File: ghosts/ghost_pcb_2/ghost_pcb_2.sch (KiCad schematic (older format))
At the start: 6 parts, among them SW1 SMT_SPDT

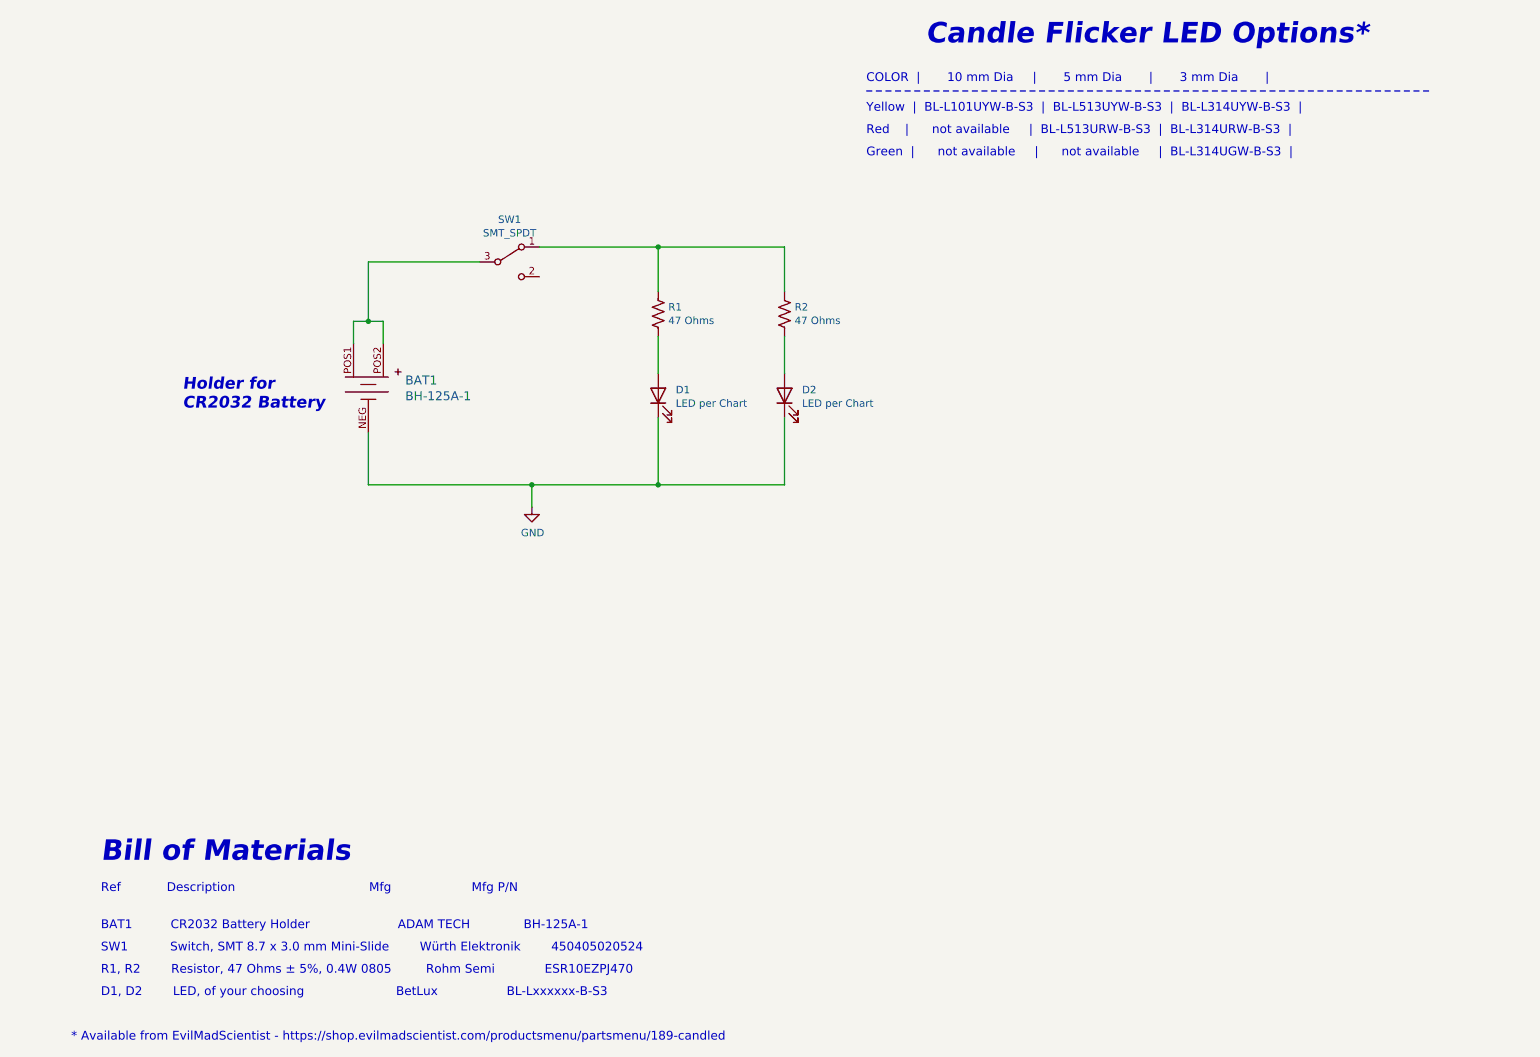
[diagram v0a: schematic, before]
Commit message: Updating all PCBS, etc.
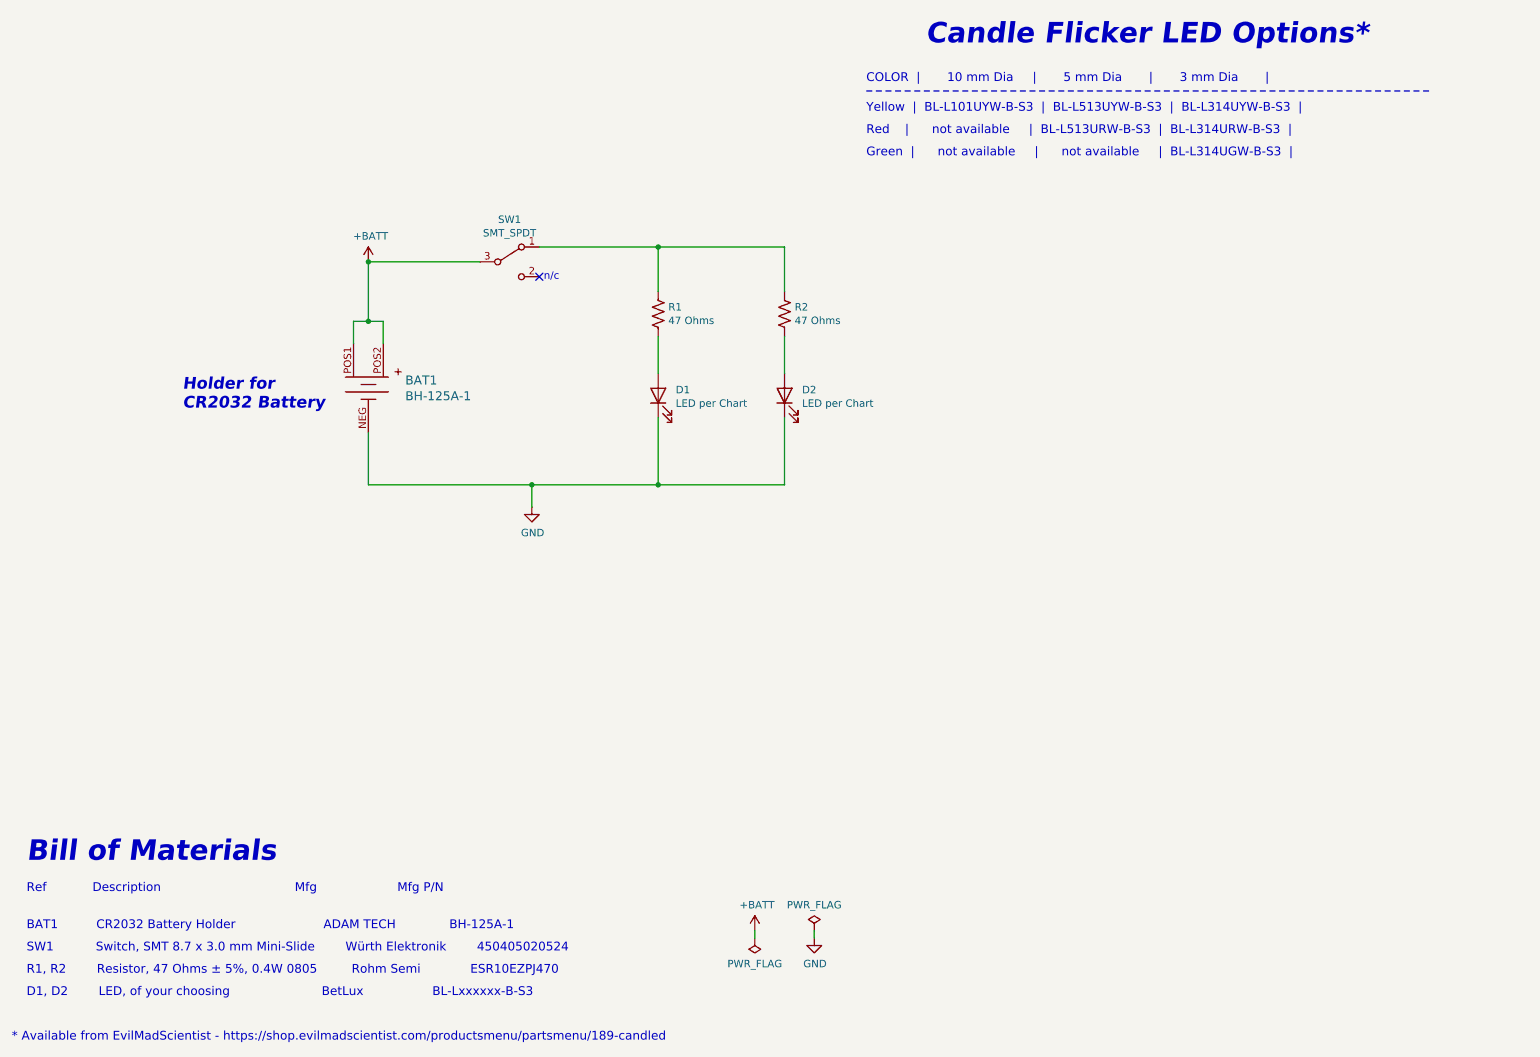
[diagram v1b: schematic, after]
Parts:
- BAT1: footprint (none) -> Battery:BatteryHolder_AdamTech_BH-125A-1
- D1, D2: footprint (none) -> LED_THT:LED_D3.0mm
- R1, R2: footprint (none) -> Resistor_SMD:R_0805_2012Metric
- SW1: footprint (none) -> Button_Switch_SMD:SMT_Mini_Slide_Switch
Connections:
- net +BATT: now reaches BAT1.POS1, BAT1.POS2, SW1.3 (B)
- no-connect marks 0 -> 1
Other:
- note added: "n/c"
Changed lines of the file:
@@
 F 0 "SW1" H 3900 2785 50  0000 C CNN
 F 1 "SMT_SPDT" H 3900 2694 50  0000 C CNN
-F 2 "" H 3900 2500 50  0001 C CNN
+F 2 "Button_Switch_SMD:SMT_Mini_Slide_Switch" H 3900 2500 50  0001 C CNN
 F 3 "" H 3900 2500 50  0001 C CNN
 	1    3900 2500
@@
 F 0 "R1" H 4968 2896 50  0000 L CNN
 F 1 "47 Ohms" H 4968 2805 50  0000 L CNN
-F 2 "" V 4940 2840 50  0001 C CNN
+F 2 "Resistor_SMD:R_0805_2012Metric" V 4940 2840 50  0001 C CNN
 F 3 "~" H 4900 2850 50  0001 C CNN
 	1    4900 2850
@@
 F 0 "D1" V 4939 3282 50  0000 R CNN
 F 1 "LED per Chart" V 4848 3282 50  0000 R CNN
-F 2 "" H 4900 3400 50  0001 C CNN
+F 2 "LED_THT:LED_D3.0mm" H 4900 3400 50  0001 C CNN
 F 3 "~" H 4900 3400 50  0001 C CNN
 	1    4900 3400
@@
 F 0 "BAT1" V 2897 3598 60  0000 L CNN
 F 1 "BH-125A-1" V 3003 3598 60  0000 L CNN
-F 2 "" H 3150 3550 60  0001 L CNN
+F 2 "Battery:BatteryHolder_AdamTech_BH-125A-1" H 3150 3550 60  0001 L CNN
 F 3 "https://app.adam-tech.com/products/download/data_sheet/197006/bh-125a-1-data-sheet.pdf" H 3150 3650 60  0001 L CNN
 F 4 "2057-BH-125A-1-ND" H 3150 3750 60  0001 L CNN "Digi-Key_PN"
@@
 Wire Wire Line
 	2950 4000 4050 4000
-Text Notes 1150 6550 0    138  Italic 28
+Text Notes 650  6550 0    138  Italic 28
 Bill of Materials
-Text Notes 1150 6750 0    59   ~ 0
+Text Notes 650  6750 0    59   ~ 0
 Ref            Description                                   Mfg                     Mfg P/N
-Text Notes 1150 7000 0    59   ~ 0
+Text Notes 650  7000 0    59   ~ 0
 BAT1          CR2032 Battery Holder                       ADAM TECH              BH-125A-1
-Text Notes 1150 7150 0    59   ~ 0
+Text Notes 650  7150 0    59   ~ 0
 SW1           Switch, SMT 8.7 x 3.0 mm Mini-Slide        Würth Elektronik        450405020524
-Text Notes 1150 7300 0    59   ~ 0
+Text Notes 650  7300 0    59   ~ 0
 R1, R2        Resistor, 47 Ohms ± 5%, 0.4W 0805         Rohm Semi             ESR10EZPJ470
-Text Notes 1150 7450 0    59   ~ 0
+Text Notes 650  7450 0    59   ~ 0
 D1, D2        LED, of your choosing                        BetLux                  BL-Lxxxxxx-B-S3
 $Comp
@@
 Text Notes 1700 3500 0    79   Italic 16
   Holder for\nCR2032 Battery
-Text Notes 950  7750 0    59   ~ 0
+Text Notes 550  7750 0    59   ~ 0
 * Available from EvilMadScientist - https://shop.evilmadscientist.com/productsmenu/partsmenu/189-candled
 $Comp
@@
 F 0 "R2" H 5818 2896 50  0000 L CNN
 F 1 "47 Ohms" H 5818 2805 50  0000 L CNN
-F 2 "" V 5790 2840 50  0001 C CNN
+F 2 "Resistor_SMD:R_0805_2012Metric" V 5790 2840 50  0001 C CNN
 F 3 "~" H 5750 2850 50  0001 C CNN
 	1    5750 2850
@@
 F 0 "D2" V 5789 3282 50  0000 R CNN
 F 1 "LED per Chart" V 5698 3282 50  0000 R CNN
-F 2 "" H 5750 3400 50  0001 C CNN
+F 2 "LED_THT:LED_D3.0mm" H 5750 3400 50  0001 C CNN
 F 3 "~" H 5750 3400 50  0001 C CNN
 	1    5750 3400
@@
 	4900 2400 5750 2400
 Connection ~ 4900 2400
+$Comp
+L power:+BATT #PWR0101
+U 1 1 616CFDC6
+P 2950 2500
+F 0 "#PWR0101" H 2950 2350 50  0001 C CNN
+F 1 "+BATT" H 2965 2673 50  0000 C CNN
+F 2 "" H 2950 2500 50  0001 C CNN
+F 3 "" H 2950 2500 50  0001 C CNN
+	1    2950 2500
+	1    0    0    -1
+$EndComp
+Connection ~ 2950 2500
+NoConn ~ 4100 2600
+Text Notes 4130 2630 0    50   ~ 0
+n/c
+$Comp
+L power:PWR_FLAG #FLG0101
+U 1 1 616D1501
+P 5950 7000
+F 0 "#FLG0101" H 5950 7075 50  0001 C CNN
+F 1 "PWR_FLAG" H 5950 7173 50  0000 C CNN
+F 2 "" H 5950 7000 50  0001 C CNN
+F 3 "~" H 5950 7000 50  0001 C CNN
+	1    5950 7000
+	1    0    0    -1
+$EndComp
+$Comp
+L power:PWR_FLAG #FLG0102
+U 1 1 616D203F
+P 5550 7050
+F 0 "#FLG0102" H 5550 7125 50  0001 C CNN
+F 1 "PWR_FLAG" H 5550 7223 50  0000 C CNN
+F 2 "" H 5550 7050 50  0001 C CNN
+F 3 "~" H 5550 7050 50  0001 C CNN
+	1    5550 7050
+	-1   0    0    1
+$EndComp
+$Comp
+L power:+BATT #PWR0102
+U 1 1 616D2410
+P 5550 7000
+F 0 "#PWR0102" H 5550 6850 50  0001 C CNN
+F 1 "+BATT" H 5565 7173 50  0000 C CNN
+F 2 "" H 5550 7000 50  0001 C CNN
+F 3 "" H 5550 7000 50  0001 C CNN
+	1    5550 7000
+	1    0    0    -1
+$EndComp
+Wire Wire Line
+	5550 7000 5550 7050
+$Comp
+L power:GND #PWR0103
+U 1 1 616D332A
+P 5950 7050
+F 0 "#PWR0103" H 5950 6800 50  0001 C CNN
+F 1 "GND" H 5955 6877 50  0000 C CNN
+F 2 "" H 5950 7050 50  0001 C CNN
+F 3 "" H 5950 7050 50  0001 C CNN
+	1    5950 7050
+	1    0    0    -1
+$EndComp
+Wire Wire Line
+	5950 7000 5950 7050
 $EndSCHEMATC
